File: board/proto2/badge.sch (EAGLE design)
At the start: 60 parts, among them IC1 TLV62569, J1 5051101092

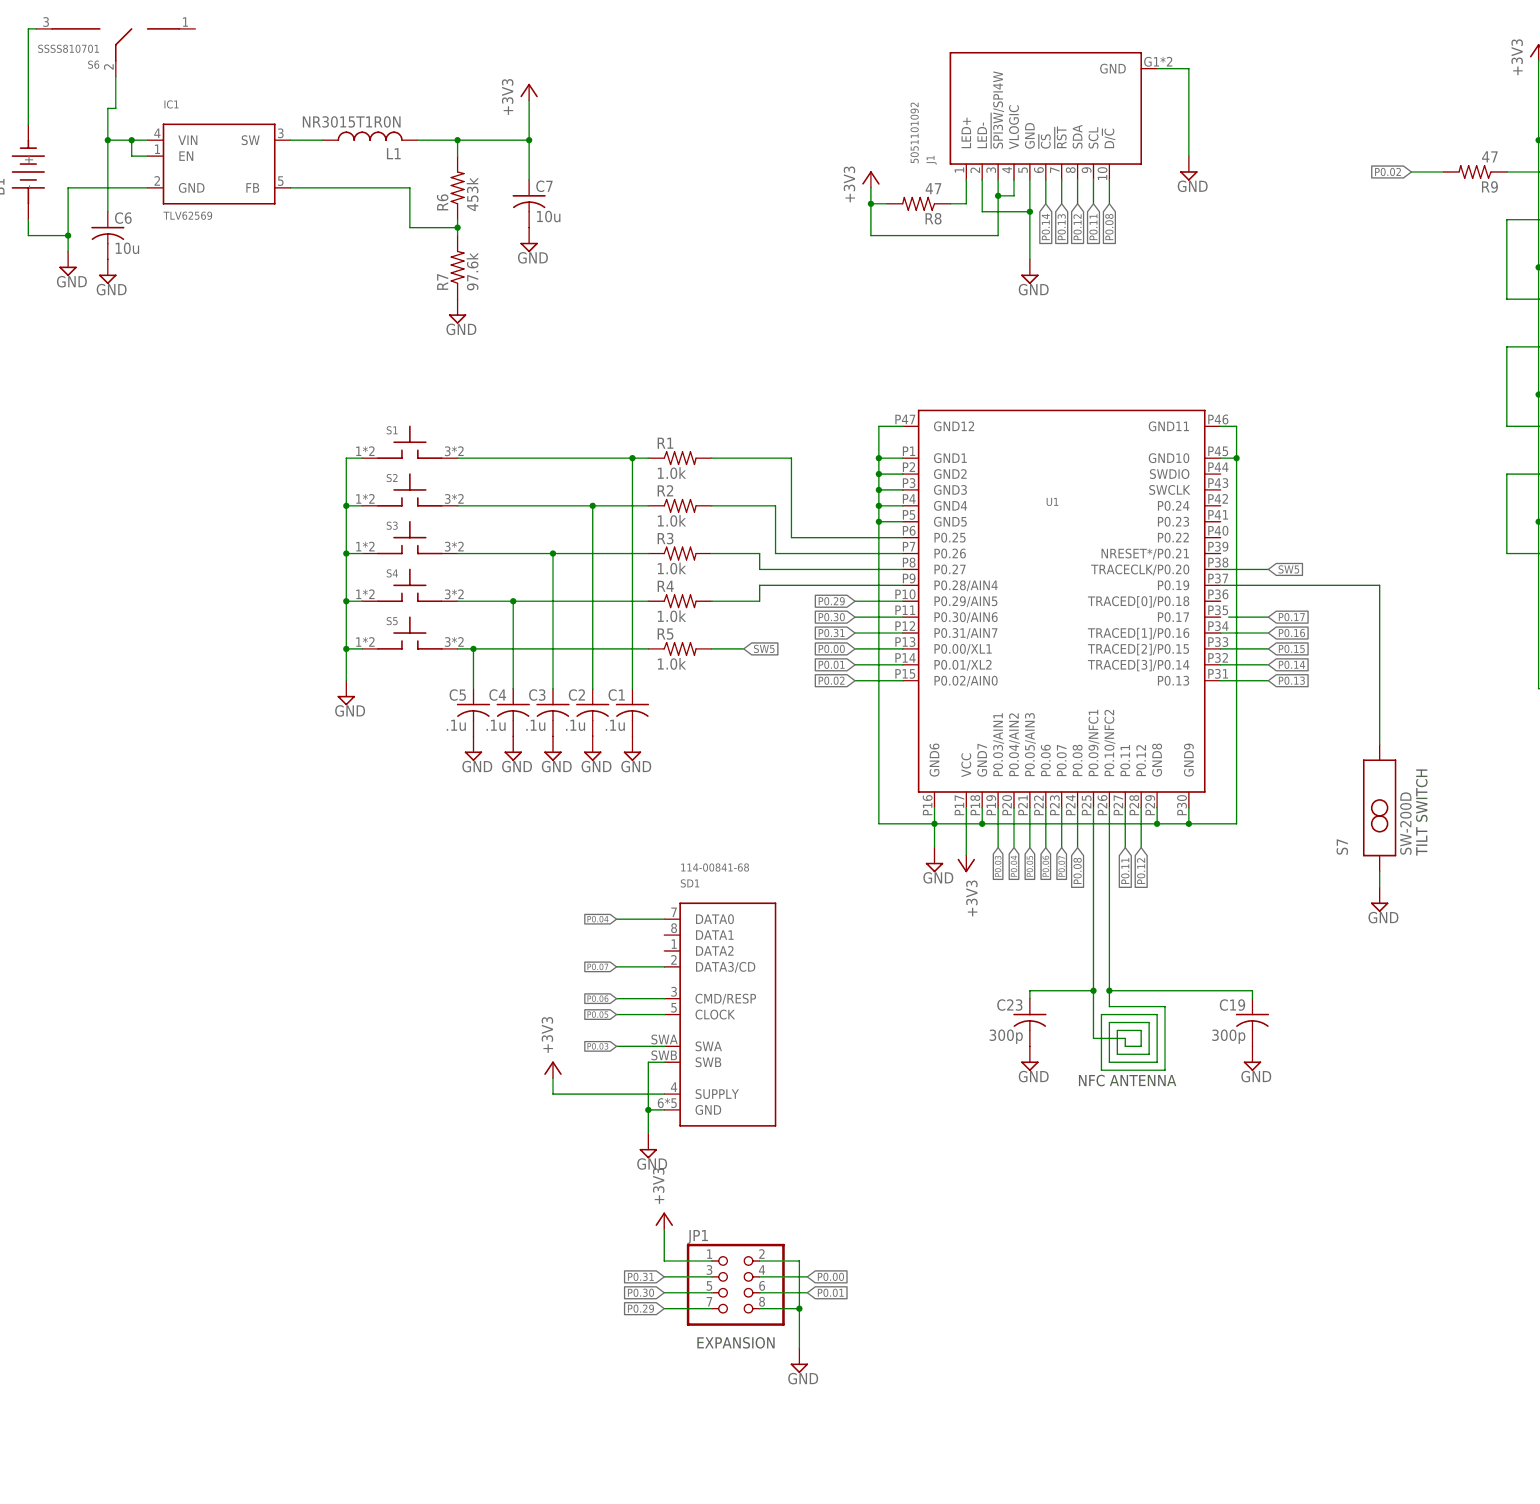
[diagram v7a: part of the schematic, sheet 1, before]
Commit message: added programming cable connector
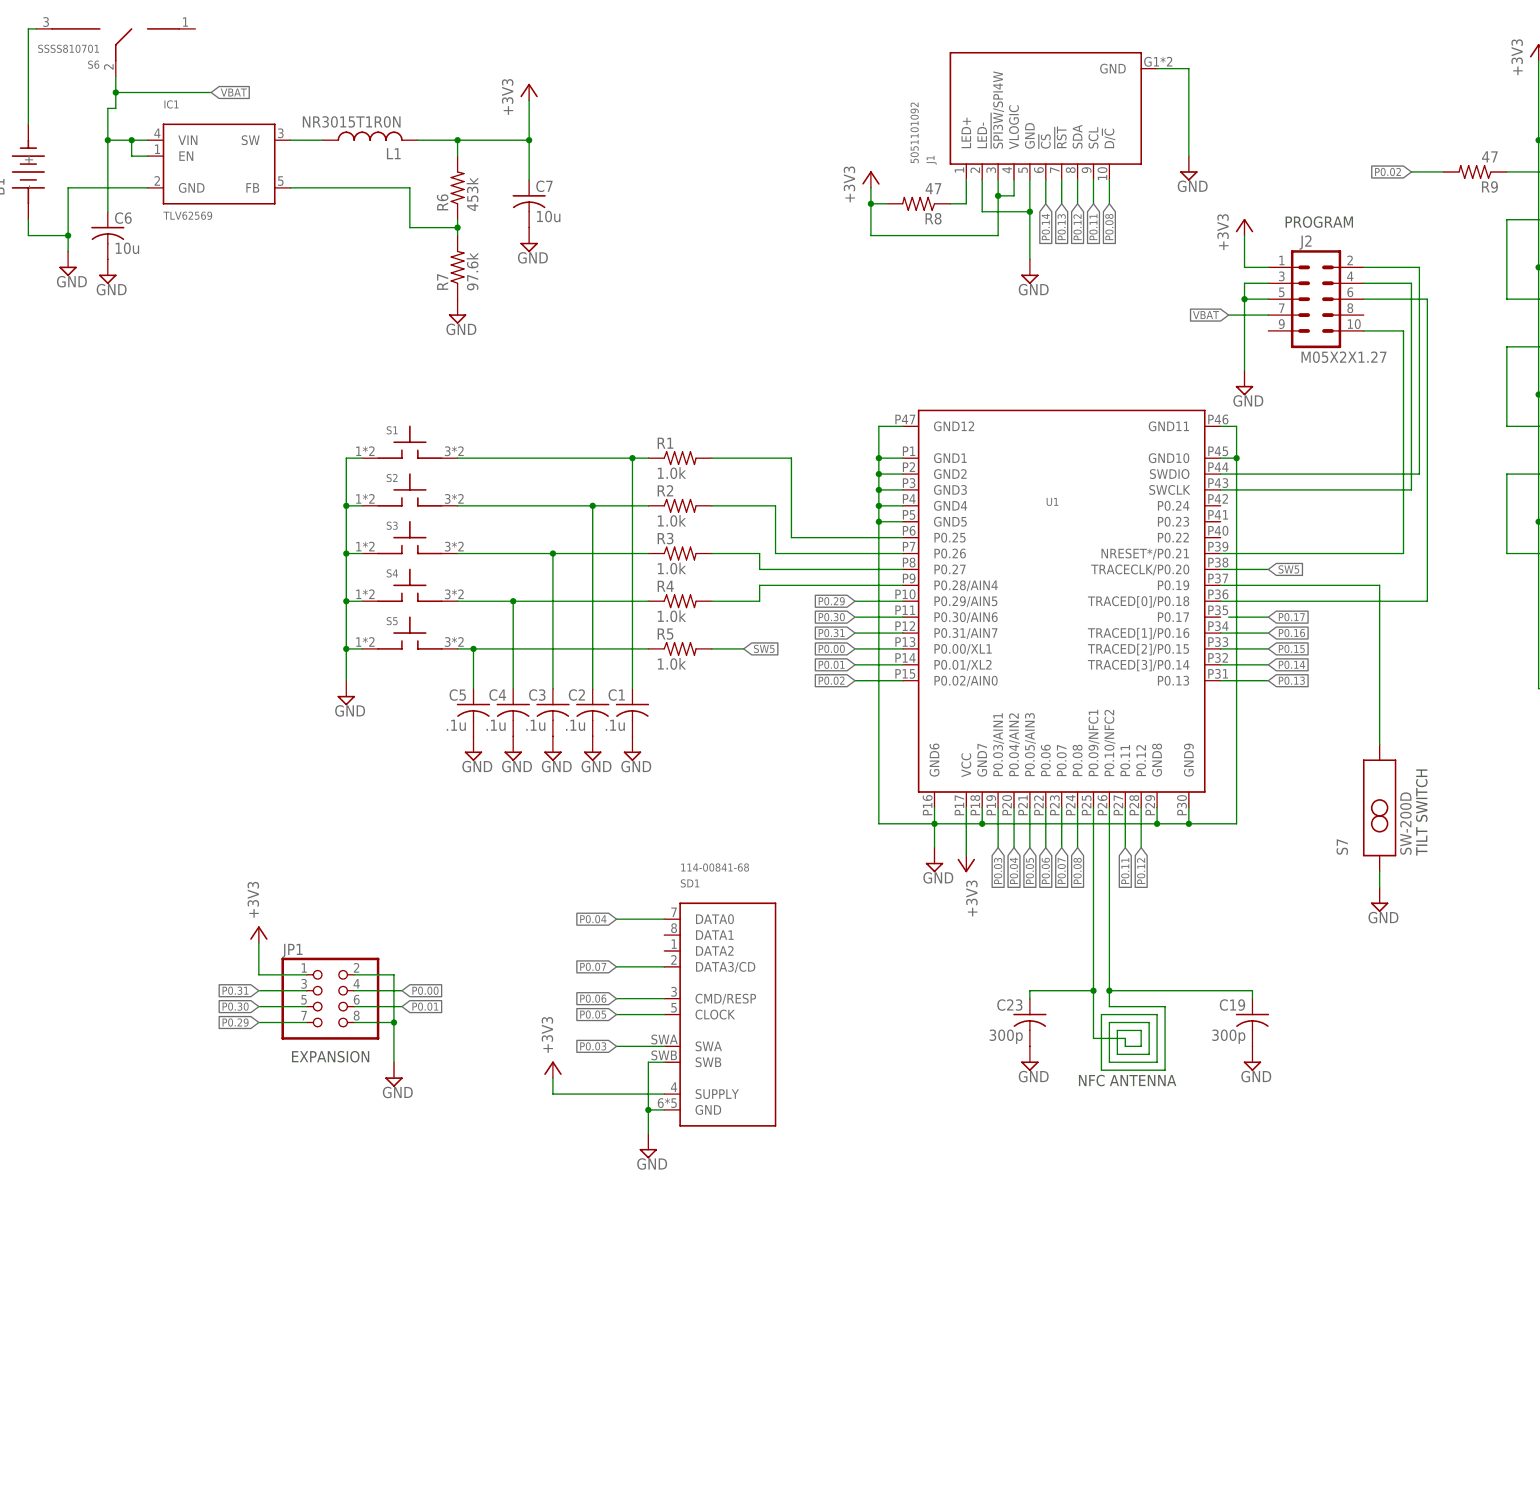
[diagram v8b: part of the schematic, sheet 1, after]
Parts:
- added J2: M05X2X1.27, badge:M05X2X1.27
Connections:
- removed net N$11: C6.1, IC1.EN, IC1.VIN, S6.2
- new net N$26: J2.2, U1.SWDIO
- new net N$31: J2.4, U1.SWCLK
- new net N$32: J2.6, U1.TRACED[0]/P0.18
- new net N$33: J2.10, U1.NRESET*/P0.21
- new net VBAT: C6.1, IC1.EN, IC1.VIN, J2.7, S6.2
- net +3V3: now also J2.1
- net GND: now also J2.3, J2.5
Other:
- note added: "PROGRAM"
- moved on the sheet: JP1
